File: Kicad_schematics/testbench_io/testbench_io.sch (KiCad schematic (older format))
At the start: 39 parts, among them J1 Conn_01x02, J2 Conn_01x02, J3 Conn_01x02, J4 DB37_Female_MountingHoles, Q5 BUK9M42-60EX, SW1 SW_SPST, SW10 SW_Push, SW11 SW_SPST, SW12 SW_SPST, SW13 SW_SPST, SW14 SW_SPST, SW2 SW_SPST, SW3 SW_Push, SW4 SW_Push, SW5 SW_Push, SW6 SW_SPST, SW7 SW_SPST, SW8 SW_SPST, SW9 SW_DIP_x08, U1 NUCLEO64-F411RE, U2 CJMCU_MCP2551

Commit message: Added footprints
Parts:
- added J105: Conn_01x02, symbol Connector_Generic:Conn_01x02
- added JP101: SolderJumper_2_Open, symbol Jumper:SolderJumper_2_Open
- added SW115: SW_Push, symbol Switch:SW_Push
- D101: renamed from D1; footprint (none) -> LED_THT:LED_D5.0mm
- D102: renamed from D2; footprint (none) -> LED_THT:LED_D5.0mm
- D103: renamed from D3; footprint (none) -> LED_THT:LED_D5.0mm
- D104: renamed from D4; footprint (none) -> LED_THT:LED_D5.0mm
- D105: renamed from D5; footprint (none) -> LED_THT:LED_D5.0mm
- D106: renamed from D6; footprint (none) -> LED_THT:LED_D5.0mm
- U101: renamed from U1; value NUCLEO64-F411RE -> NUCLEO64-F476RG
- renumbered J1 to J101, J2 to J102, J3 to J103, J4 to J104, Q5 to Q101, R1 to R101, R2 to R102, R3 to R103, R8 to R104, R4 to R105, R5 to R106, R11 to R107, R12 to R108, RV1 to RV101, RV2 to RV102, RV3 to RV103, RV4 to RV104, SW1 to SW101, SW2 to SW102, SW3 to SW103, SW4 to SW104, SW5 to SW105, SW6 to SW106, SW7 to SW107, SW8 to SW108, SW9 to SW109, SW10 to SW110, SW11 to SW111, SW12 to SW112, SW13 to SW113, SW14 to SW114, U2 to U102
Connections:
- net labels added: MCU_5V, Reset
- net labels removed: 5V, TRM_VCC, VDD
- wire segments 162 -> 154
- no-connect marks 0 -> 60
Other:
- moved on the sheet: R104

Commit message: Started with layout
Signed-off-by: Mojitas <47667093+Mojitas@users.noreply.github.com>
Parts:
- removed J101, J105: Conn_01x02, symbol Connector_Generic:Conn_01x02
- added J1: Conn_01x02, Connector_JST:JST_XH_S2B-XH-A-1_1x02_P2.50mm_Horizontal, symbol Connector_Generic:Conn_01x02
- J102, J103: footprint (none) -> Connector_JST:JST_XH_S2B-XH-A-1_1x02_P2.50mm_Horizontal
- J104: footprint (none) -> Connector_Dsub:DSUB-37_Female_EdgeMount_P2.77mm
- JP101: footprint (none) -> Jumper:SolderJumper-2_P1.3mm_Open_Pad1.0x1.5mm
- Q101: footprint Package_TO_SOT_SMD:LFPAK33 -> Package_TO_SOT_SMD:TO-252-2
- R101, R102, R103, R104, R105, R106, R107, R108: footprint (none) -> Resistor_SMD:R_0603_1608Metric
- RV101, RV102, RV103, RV104: footprint (none) -> Potentiometer_THT:Potentiometer_Bourns_PTV09A-1_Single_Vertical
- SW101, SW102, SW106, SW107, SW108, SW111, SW112, SW113, SW114: footprint (none) -> Solar_team:MTS-102-A2
- SW103, SW104, SW105, SW110, SW115: footprint (none) -> Button_Switch_THT:SW_PUSH-12mm
- SW109: footprint (none) -> Package_DIP:DIP-16_W7.62mm
- U101: footprint Module:ST_Morpho_Connector_144_STLink -> Solar_team:MODULE_NUCLEO-F446RE
- U102: footprint (none) -> Solar_team:CJMCU_2551
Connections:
- net labels removed: Uart_rx, Uart_tx
- wire segments 154 -> 152
- no-connect marks 60 -> 62
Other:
- moved on the sheet: JP101

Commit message: Pcb-layout is on the way
Signed-off-by: Mojitas <47667093+Mojitas@users.noreply.github.com>
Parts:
- removed Q101: BUK9M42-60EX, Package_TO_SOT_SMD:TO-252-2, symbol Transistor_FET:BUK9M42-60EX
- added Q101: IPD50R380CE, Package_TO_SOT_SMD:TO-252-2, symbol Transistor_FET:IPD50R380CE
- U101: footprint Solar_team:MODULE_NUCLEO-F446RE -> Solar_team:MODULE_NUCLEO-F476RG
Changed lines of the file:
@@
 F 0 "U101" H 2200 7581 50  0000 C CNN
 F 1 "NUCLEO64-F476RG" H 2200 7490 50  0000 C CNN
-F 2 "Solar_team:MODULE_NUCLEO-F446RE" H 2750 3500 50  0001 L CNN
+F 2 "Solar_team:MODULE_NUCLEO-F476RG" H 2750 3500 50  0001 L CNN
 F 3 "http://www.st.com/st-web-ui/static/active/en/resource/technical/document/data_brief/DM00105918.pdf" H 1300 4000 50  0001 C CNN
 	1    2200 5400
@@
 	1    7250 1700
 	0    1    1    0
-$EndComp
-$Comp
-L Transistor_FET:BUK9M42-60EX Q101
-U 1 1 603A338F
-P 7400 1450
-F 0 "Q101" H 7300 1600 50  0000 L CNN
-F 1 "BUK9M42-60EX" V 7700 1250 50  0000 L CNN
-F 2 "Package_TO_SOT_SMD:TO-252-2" H 7600 1375 50  0001 L CIN
-F 3 "https://assets.nexperia.com/documents/data-sheet/BUK9M42-60E.pdf" V 7400 1450 50  0001 L CNN
-	1    7400 1450
-	1    0    0    -1
 $EndComp
 Wire Notes Line
@@
 	1    0    0    -1
 $EndComp
+$Comp
+L Transistor_FET:IPD50R380CE Q?
+U 1 1 60108F48
+P 7400 1450
+AR Path="/6001478F/60108F48" Ref="Q?"  Part="1"
+AR Path="/60108F48" Ref="Q101"  Part="1"
+F 0 "Q101" H 7605 1496 50  0000 L CNN
+F 1 "IPD50R380CE" H 7605 1405 50  0000 L CNN
+F 2 "Package_TO_SOT_SMD:TO-252-2" H 7600 1375 50  0001 L CIN
+F 3 "https://www.infineon.com/dgdl/Infineon-IPD50R380CE-DS-v02_01-en.pdf?fileId=db3a30433ecb86d4013ed0a2ef580f38" H 7400 1450 50  0001 L CNN
+	1    7400 1450
+	1    0    0    -1
+$EndComp

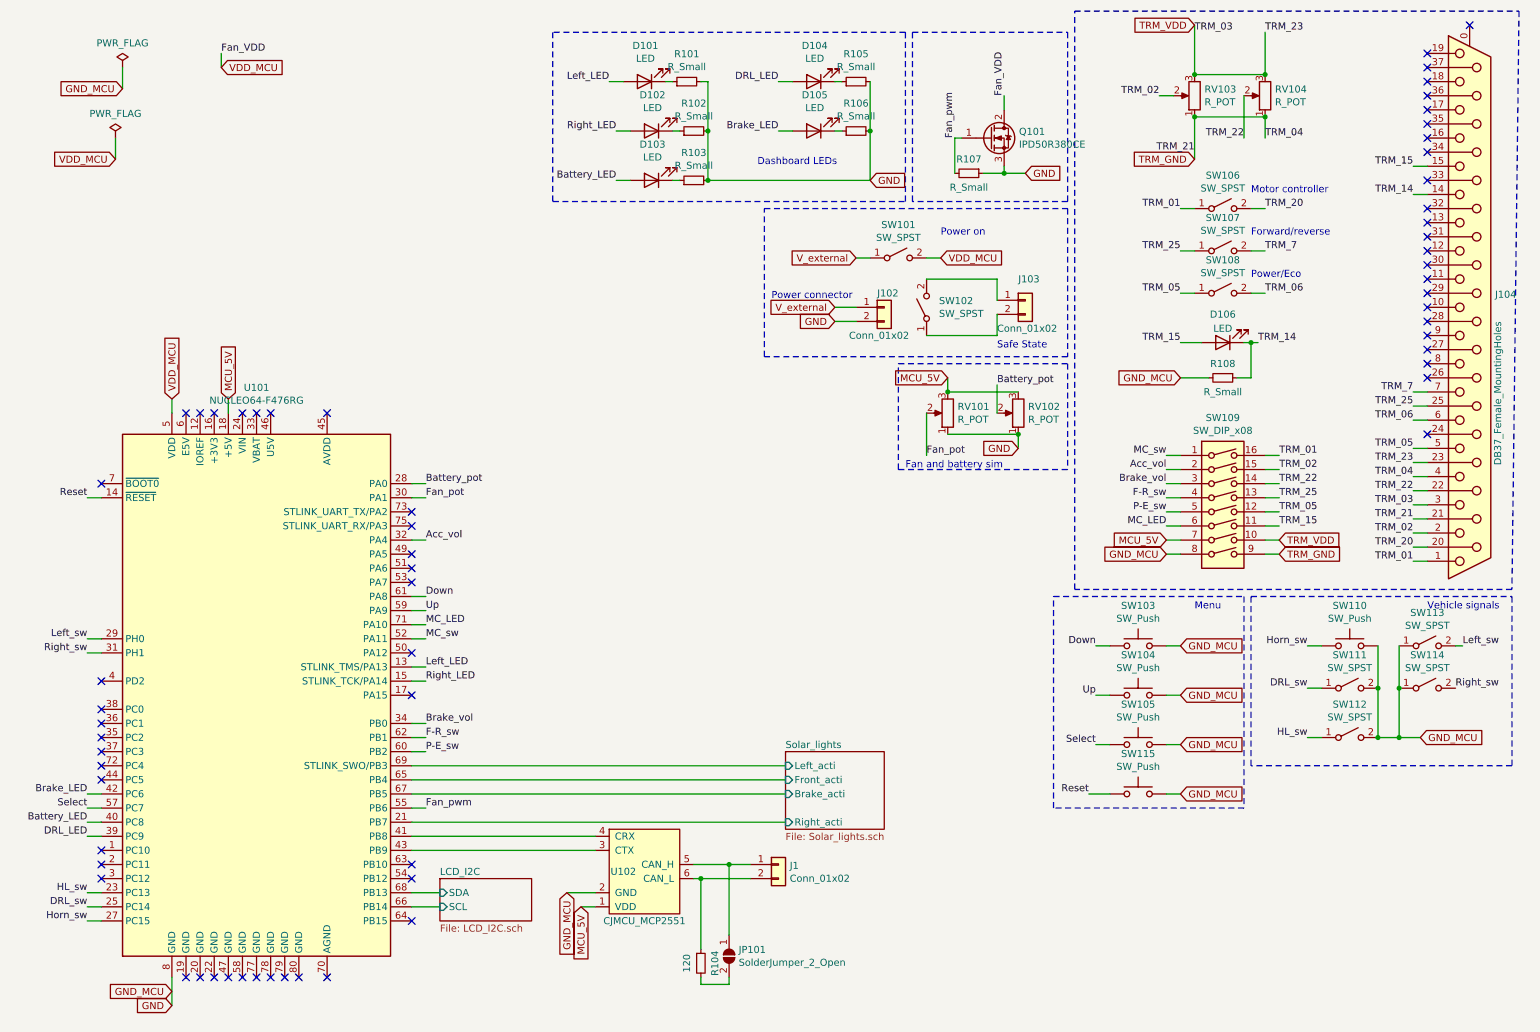
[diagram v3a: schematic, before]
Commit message: Routing done and power planes added
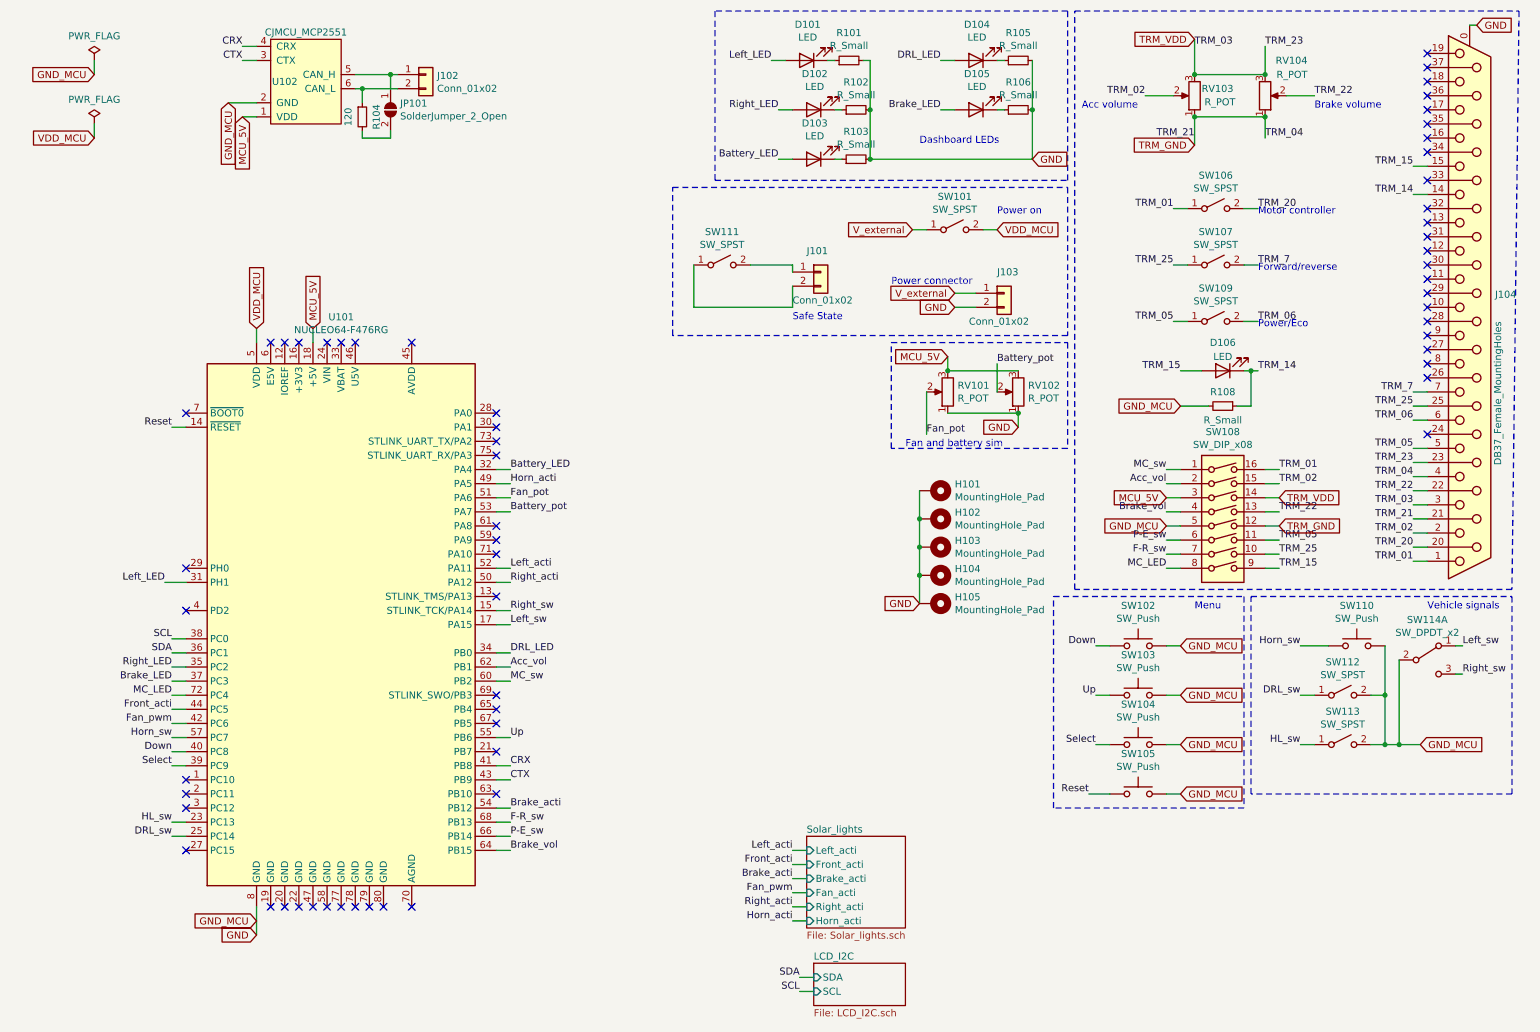
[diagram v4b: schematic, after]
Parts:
- removed Q101: IPD50R380CE, Package_TO_SOT_SMD:TO-252-2, symbol Transistor_FET:IPD50R380CE
- removed R107: R_Small, Resistor_SMD:R_0603_1608Metric, symbol Device:R_Small
- removed SW102, SW108, SW114: SW_SPST, Solar_team:MTS-102-A2, symbol Switch:SW_SPST
- added H101, H102, H103, H104, H105: MountingHole_Pad, MountingHole:MountingHole_3.2mm_M3_Pad_Via, symbol Mechanical:MountingHole_Pad
- added SW109: SW_SPST, Solar_team:RND-Slide-Switch, symbol Switch:SW_SPST
- added SW114: SW_DPDT_x2, Solar_team:RND-Slide-Switch, symbol Switch:SW_DPDT_x2
- J104: footprint Connector_Dsub:DSUB-37_Female_EdgeMount_P2.77mm -> Connector_Dsub:DSUB-37_Female_Horizontal_P2.77x2.84mm_EdgePinOffset7.70mm_Housed_MountingHolesOffset9.12mm
- SW101, SW106, SW107, SW111, SW112, SW113: footprint Solar_team:MTS-102-A2 -> Solar_team:RND-Slide-Switch
- renumbered J103 to J101, J1 to J102, J102 to J103, SW103 to SW102, SW104 to SW103, SW105 to SW104, SW115 to SW105, SW109 to SW108
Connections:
- net LCD_I2C/SCL is gone; now on net P-E_sw: U101.66 (PB14)
- net LCD_I2C/SDA is gone; now on net F-R_sw: U101.68 (PB13)
- net Acc_vol: now also U101.62 (PB1); no longer U101.32 (PA4)
- net Battery_LED: now also U101.32 (PA4); no longer U101.40 (PC8)
- net Battery_pot: now also U101.53 (PA7); no longer U101.28 (PA0)
- net Brake_LED: now also U101.37 (PC3); no longer U101.42 (PC6)
- net Brake_vol: now also SW108.4, U101.64 (PB15); no longer SW108.3, U101.34 (PB0)
- net DRL_LED: now also U101.34 (PB0); no longer U101.39 (PC9)
- net DRL_sw: now also SW112.1 (A); no longer SW111.1 (A)
- net Down: now also U101.40 (PC8); no longer U101.61 (PA8)
- net F-R_sw: now also SW108.7; no longer SW108.4, U101.62 (PB1)
- net Fan_pot: now also U101.51 (PA6); no longer U101.30 (PA1)
- net Fan_pwm: now also U101.42 (PC6); no longer U101.55 (PB6)
- net GND: now also J104.0 (PAD), SW108.5, SW113.2 (B), H101.1, H102.1, H103.1, H104.1, H105.1, SW114.2 (B); no longer SW108.8, SW111.2 (B), SW113.1 (A)
- net HL_sw: now also SW113.1 (A); no longer SW112.1 (A)
- net Horn_sw: now also U101.57 (PC7); no longer U101.27 (PC15)
- net Left_LED: now also U101.31 (PH1); no longer U101.13 (STLINK_TMS/PA13)
- net Left_sw: now also U101.17 (PA15), SW114.1 (A); no longer SW113.2 (B), U101.29 (PH0)
- net MCU_5V: now also SW108.3; no longer SW108.7
- net MC_LED: now also SW108.8, U101.72 (PC4); no longer SW108.6, U101.71 (PA10)
- net MC_sw: now also U101.60 (PB2); no longer U101.52 (PA11)
- net P-E_sw: now also SW108.6; no longer SW108.5, U101.60 (PB2)
- net Right_LED: now also U101.35 (PC2); no longer U101.15 (STLINK_TCK/PA14)
- net Right_sw: now also U101.15 (STLINK_TCK/PA14), SW114.3 (C); no longer U101.31 (PH1)
- net Select: now also U101.39 (PC9); no longer U101.57 (PC7)
- net TRM_05: now also SW108.11, SW109.1 (A); no longer SW108.12
- net TRM_06: now also SW109.2 (B)
- net TRM_15: now also SW108.9; no longer SW108.11
- net TRM_22: now also SW108.13; no longer SW108.14
- net TRM_25: now also SW108.10; no longer SW108.13
- net TRM_GND: now also SW108.12; no longer SW108.9
- net TRM_VDD: now also SW108.14; no longer SW108.10
- net Up: now also U101.55 (PB6); no longer U101.59 (PA9)
- net SDA: now reaches U101.36 (PC1)
- net SCL: now reaches U101.38 (PC0)
- net CRX: now reaches U101.41 (PB8), U102.4 (CRX)
- net CTX: now reaches U101.43 (PB9), U102.3 (CTX)
- net Front_acti: now reaches U101.44 (PC5)
- net Horn_acti: now reaches U101.49 (PA5)
- net Right_acti: now reaches U101.50 (PA12)
- net Brake_acti: now reaches U101.54 (PB12)
- net at J101.1 (Pin_1): now also SW111.2 (B)
- net at J101.2 (Pin_2): now also SW111.1 (A)
- net Solar_lights/Brake_acti: no longer names the net of U101.67 (PB5)
- net Solar_lights/Front_acti: no longer names the net of U101.65 (PB4)
- net Solar_lights/Left_acti: no longer names the net of U101.69 (STLINK_SWO/PB3)
- net Solar_lights/Right_acti: no longer names the net of U101.21 (PB7)
- new net Left_acti: U101.52 (PA11)
- no-connect marks 62 -> 60
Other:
- note added: "Acc volume\n"
- note added: "Brake volume\n"
- moved on the sheet: D101, D102, D103, D104, D105, D106, J101, J102, J103, JP101, R101, R102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

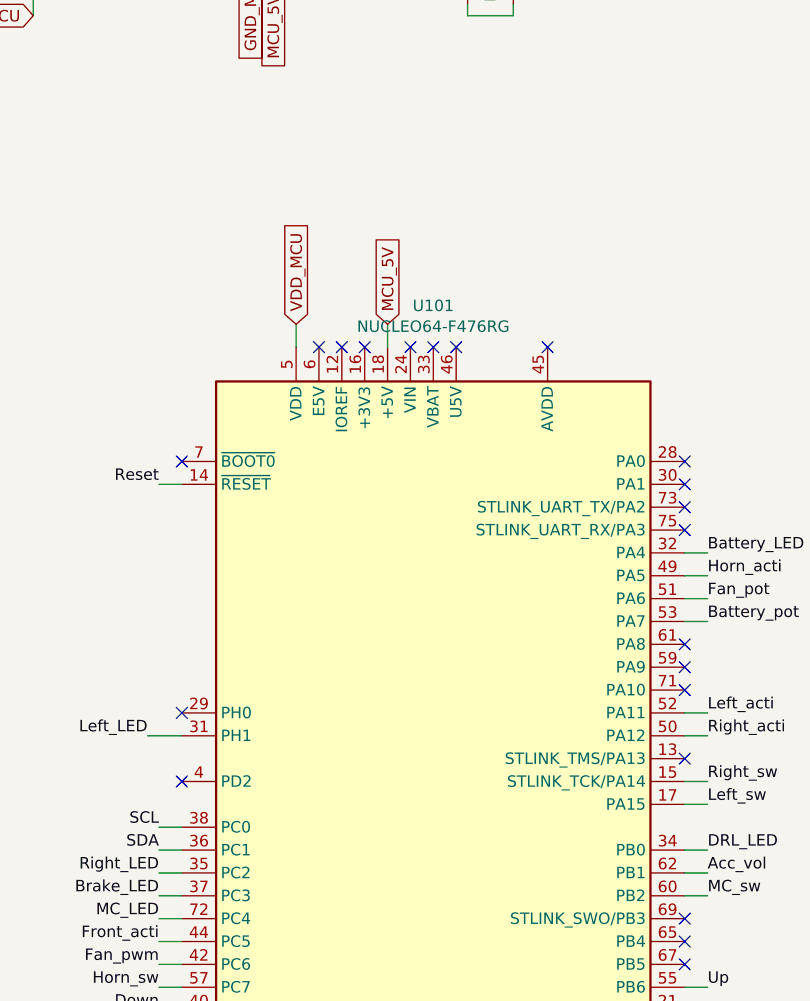
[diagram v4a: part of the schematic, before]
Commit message: Removed redundant tracks
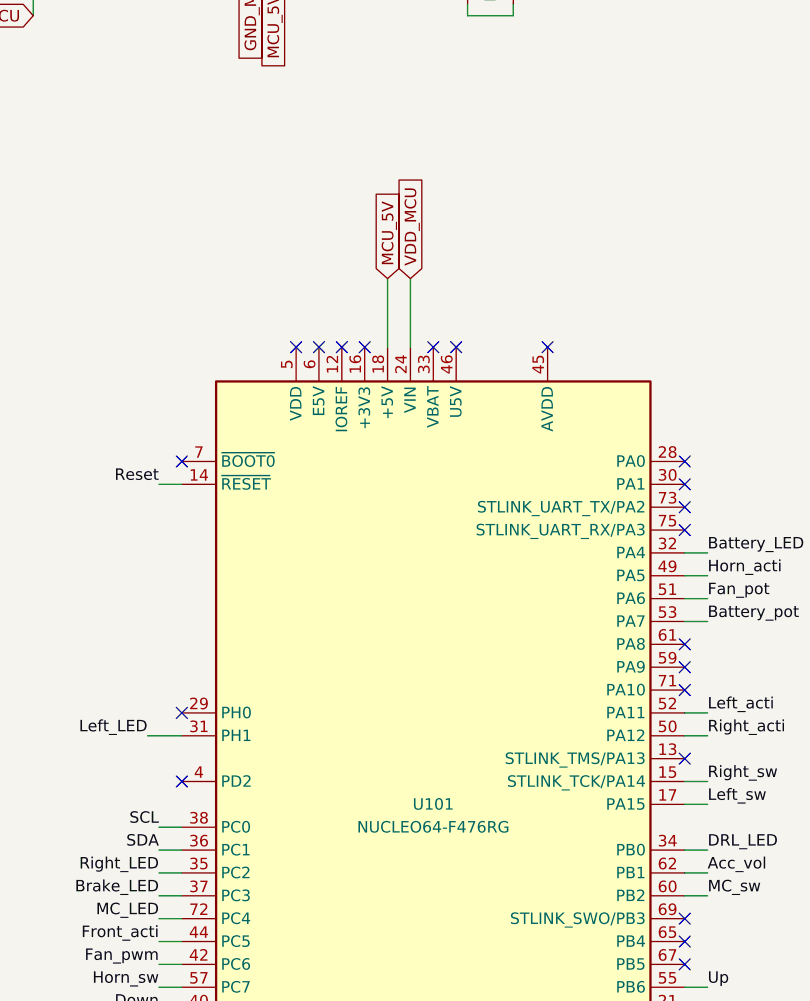
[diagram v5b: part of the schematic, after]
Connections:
- net VDD_MCU: now also U101.24 (VIN); no longer U101.5 (VDD)
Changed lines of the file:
@@
 U 1 1 5FF2E5E7
 P 2800 4900
-F 0 "U101" H 2800 7081 50  0000 C CNN
-F 1 "NUCLEO64-F476RG" H 2800 6990 50  0000 C CNN
+F 0 "U101" H 2800 4900 50  0000 C CNN
+F 1 "NUCLEO64-F476RG" H 2800 4800 50  0000 C CNN
 F 2 "Solar_team:MODULE_NUCLEO-F476RG" H 3350 3000 50  0001 L CNN
 F 3 "http://www.st.com/st-web-ui/static/active/en/resource/technical/document/data_brief/DM00105918.pdf" H 1900 3500 50  0001 C CNN
@@
 Wire Wire Line
 	4000 4800 3900 4800
-Text GLabel 2200 2800 1    50   Input ~ 0
+Text GLabel 2700 2600 1    50   Input ~ 0
 VDD_MCU
 Wire Wire Line
-	2200 2800 2200 2900
+	2700 2600 2700 2900
 Text GLabel 2200 7000 0    50   Input ~ 0
 GND_MCU
@@
 NoConn ~ 3900 4400
 Wire Wire Line
-	2600 2800 2600 2900
-Text GLabel 2600 2800 1    50   Input ~ 0
+	2600 2600 2600 2900
+Text GLabel 2600 2600 1    50   Input ~ 0
 MCU_5V
 Text GLabel 7100 3000 0    50   Input ~ 0
@@
 NoConn ~ 2900 2900
 NoConn ~ 2800 2900
-NoConn ~ 2700 2900
+NoConn ~ 2200 2900
 NoConn ~ 2500 2900
 NoConn ~ 2400 2900
